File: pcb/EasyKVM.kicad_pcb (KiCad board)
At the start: 4 copper layers, 75 x 75 mm, 58 parts, among them J1 USB_A, J4 USB_B_Micro, J5 USB_B_Micro, J6 HDMI_A, J7 USB_B_Micro, J8 HDMI_A, J9 USB_A, Q1 MMBT3904, Q2 MMBT3904, Q3 BSS138, Q4 BSS138, Q5 BSS138, SW1 RESET, U1 SP0503BAHT, U2 LM3525M-H, U3 SP0503BAHT, U4 MAX4999ETJ+, U5 CP2102N-Axx-xQFN24, U6 ESP32-S3-WROOM-1, U7 SP0503BAHT, U9 AP7361C-33E

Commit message: routing start
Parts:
- added R2: 100K, Resistor_SMD:R_0603_1608Metric, F.Cu at (111.0, 104.5)
- added R3: 100K, Resistor_SMD:R_0603_1608Metric, F.Cu at (111.0, 106.6)
- added R5: 1K, Resistor_SMD:R_0603_1608Metric, F.Cu at (114.2, 108.2)
- moved D4 21.5 mm to (100.5, 138.0), turned to 90 degrees
- moved Q3 20.8 mm to (116.8, 126.1)
- moved R8 13.0 mm to (145.3, 106.5)
- moved R28 8.12 mm to (112.0, 148.4)
- moved C21 8.12 mm to (119.4, 154.9)
- moved Q1 6.51 mm to (141.4, 124.8)
- moved Q4 6.06 mm to (116.8, 130.6)
- moved C27 5.57 mm to (149.1, 123.9), turned to 90 degrees
- moved R31 5.23 mm to (145.6, 123.9), turned to -90 degrees
- moved Q2 5.22 mm to (141.4, 110.3), turned to 180 degrees
- moved R23 4.74 mm to (145.3, 110.4), turned to -90 degrees
- moved R1 2.62 mm to (114.2, 105.0), turned to 0 degrees
- moved D5 2.20 mm to (161.7, 103.9), turned to 0 degrees
- moved C2 2.05 mm to (150.9, 156.9)
- moved C30 2.03 mm to (152.3, 159.4), turned to 180 degrees
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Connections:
- D5 pad 1: ESD_PC1_USB_N -> ESD_PC1_USB_P
- D5 pad 2: ESD_PC1_USB_P -> ESD_PC1_USB_N
- D6 pad 1: ESD_PC2_USB_N -> ESD_PC2_USB_P
- D6 pad 2: ESD_PC2_USB_P -> ESD_PC2_USB_N
- U2 pad 1: KVM_ENABLE -> USB_ENABLE
- U2 pad 2: unconnected-(U2-Pad2) -> OVER_CURRENT
- U3 pad 3: HUB_USB_N -> HUB_USB_P
- U3 pad 4: HUB_USB_P -> HUB_USB_N
- U6 pad 4: unconnected-(U6-Pad4) -> OVER_CURRENT
- U6 pad 7: unconnected-(U6-Pad7) -> Net-(R5-Pad2)
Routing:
- net CHIP_PU: track 0.00 -> 88.3 mm, vias 0 -> 4
- net ESD_DDC_SDA: track 0.00 -> 57.7 mm, vias 0 -> 2
- net ESD_DDC_SCL: track 0.00 -> 56.1 mm, vias 0 -> 2
- net ESD_PC2_USB_N: track 0.00 -> 49.4 mm
- net ESD_PC2_USB_P: track 0.00 -> 49.3 mm
- net KBD_USB_N: track 0.00 -> 48.9 mm, vias 0 -> 2
- net KBD_USB_P: track 0.00 -> 48.7 mm, vias 0 -> 2
- net HDMI_5V: track 0.00 -> 45.2 mm
- net ESD_PC1_USB_N: track 0.00 -> 43.5 mm
- net ESD_PC1_USB_P: track 0.00 -> 43.4 mm
- net DDC_SCL: track 0.00 -> 42.5 mm, vias 0 -> 2
- net Net-(J6-Pad19): track 0.00 -> 40.3 mm
- net HDMI_CLK_P: track 0.00 -> 39.8 mm, vias 0 -> 2
- net DDC_SDA: track 0.00 -> 39.4 mm, vias 0 -> 2
- net ESD_USB_N: track 0.00 -> 39.2 mm, vias 0 -> 2
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
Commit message: pcb wip
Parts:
- moved R32 33.9 mm to (132.5, 122.4)
- moved R34 11.3 mm to (155.5, 120.7), turned to 0 degrees
- moved C17 11.1 mm to (155.5, 123.7), turned to 180 degrees
- moved C21 8.25 mm to (126.5, 150.7)
- moved C20 7.04 mm to (165.7, 119.5)
- moved C30 6.20 mm to (158.2, 161.5), turned to 90 degrees
- moved R36 6.17 mm to (161.1, 165.9), turned to 0 degrees
- moved R35 4.92 mm to (163.8, 160.6), turned to 180 degrees
- moved R3 3.82 mm to (108.6, 109.5)
- moved R2 3.45 mm to (108.6, 106.9)
- moved C28 2.46 mm to (113.8, 102.6), turned to 180 degrees
- moved Q5 2.37 mm to (161.1, 162.9)
- moved D1 2.33 mm to (165.7, 121.6)
- moved R22 2.26 mm to (165.7, 123.8)
- moved C11 1.99 mm to (154.3, 101.3)
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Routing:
- net GND: track 0.00 -> 168.0 mm, vias 0 -> 52
- net VBUS: track 14.8 -> 133.6 mm
- net Net-(Q5-Pad2): track 0.00 -> 63.7 mm, vias 0 -> 2
- net KVM_SELECT: track 0.00 -> 60.7 mm, vias 0 -> 2
- net OVER_CURRENT: track 0.00 -> 57.6 mm, vias 0 -> 2
- net KVM_ENABLE: track 0.00 -> 55.5 mm, vias 0 -> 2
- net USB_ENABLE: track 0.00 -> 54.7 mm, vias 0 -> 2
- net 3.3V: track 0.00 -> 35.5 mm, vias 0 -> 15
- net Net-(R34-Pad2): track 0.00 -> 23.6 mm, vias 0 -> 2
- net Net-(D3-Pad2): track 0.00 -> 20.5 mm
- net ESD_DDC_SDA: track 57.7 -> 49.6 mm
- net DDC_SCL: track 42.5 -> 48.5 mm
- net HUB_VBUS: track 21.2 -> 25.5 mm
- net DDC_SDA: track 39.4 -> 43.6 mm
- net RGB: track 0.00 -> 4.12 mm
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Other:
- board text added: "Easy KVM R1.0"

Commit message: R1
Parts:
- moved C2 0.30 mm to (150.6, 157.0)
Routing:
- net HDMI_D2_P: track 32.0 -> 38.6 mm
- net HDMI_D2_N: track 32.3 -> 38.6 mm
- net HDMI_D1_N: track 34.7 -> 38.7 mm
- net HDMI_D1_P: track 34.8 -> 38.7 mm
- net HDMI_D0_P: track 36.8 -> 38.5 mm
- net HDMI_D0_N: track 37.2 -> 38.6 mm
- net GND: track 168.0 -> 167.4 mm
- net KBD_USB_N: track 48.9 -> 49.5 mm

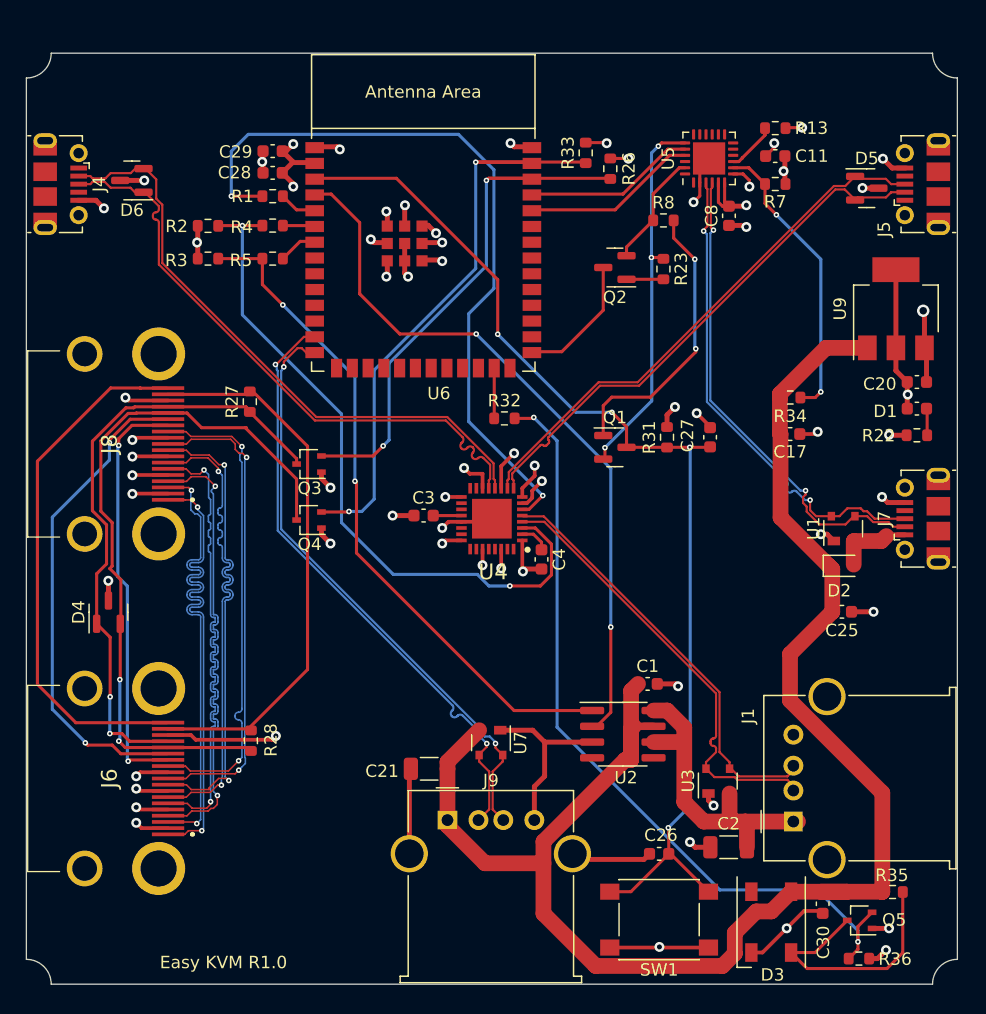
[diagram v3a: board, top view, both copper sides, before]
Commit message: design bugs case update software bugs
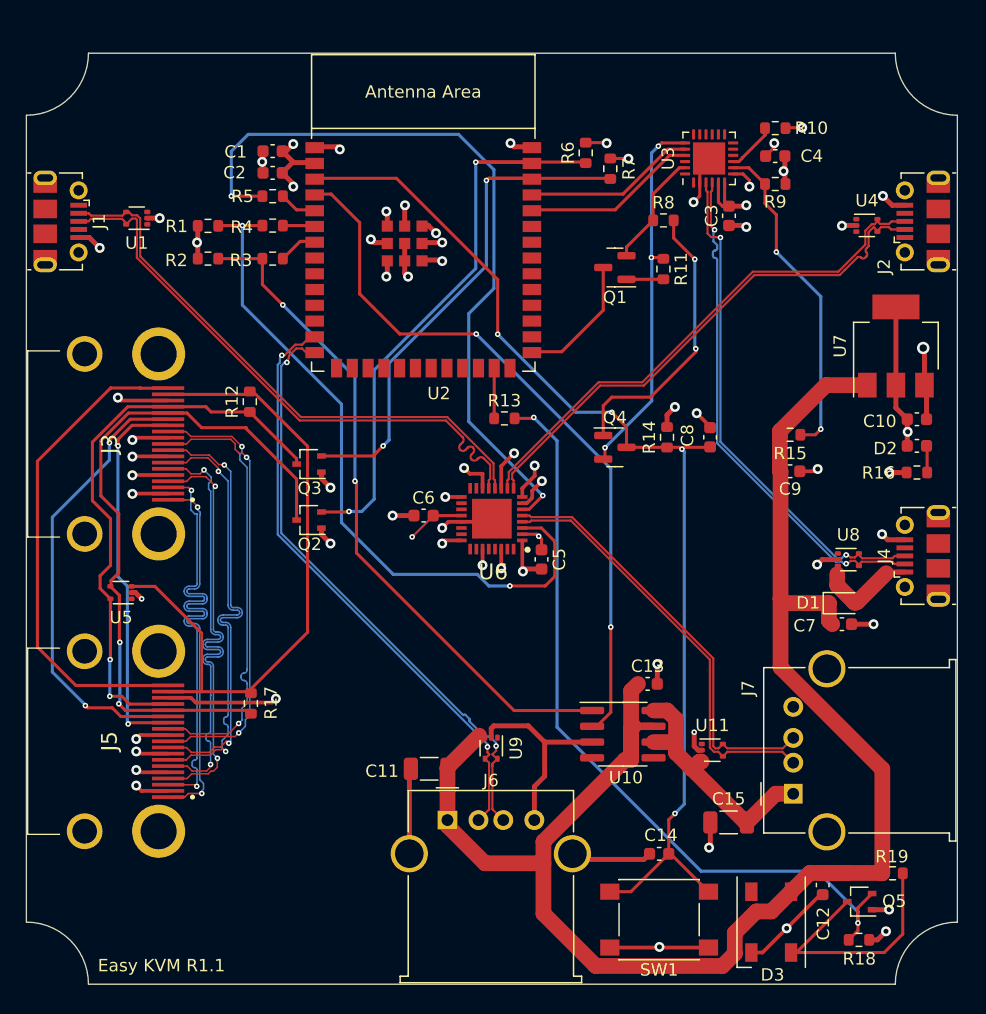
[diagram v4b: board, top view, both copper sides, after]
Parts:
- removed D4, D5, D6: SP0502BAHT, Package_TO_SOT_SMD:SOT-23
- removed the U3 at (149.7, 151.6)
- removed the U7 at (131.4, 148.5)
- added U11: SP3003-02XTG, Package_TO_SOT_SMD:Diodes_SOT-553, F.Cu at (149.3, 149.2)
- added U4: SP3003-02XTG, Package_TO_SOT_SMD:Diodes_SOT-553, F.Cu at (161.7, 106.9)
- added U5: SP3003-02XTG, Package_TO_SOT_SMD:Diodes_SOT-553, F.Cu at (101.6, 136.5)
- added U8: SP3003-02XTG, Package_TO_SOT_SMD:Diodes_SOT-553, F.Cu at (160.2, 133.8)
- added U9: SP3003-02XTG, Package_TO_SOT_SMD:Diodes_SOT-553, F.Cu at (131.4, 149.0)
- U1: value SP0503BAHT -> SP3003-02XTG; footprint Package_TO_SOT_SMD:SOT-143 -> Package_TO_SOT_SMD:Diodes_SOT-553
- moved U1 62.2 mm to (102.9, 106.3), turned to 180 degrees
- moved C10 3.00 mm to (165.7, 122.5)
- moved C9 3.00 mm to (155.5, 126.7)
- moved D1 3.00 mm to (159.7, 137.3)
- moved D2 3.00 mm to (165.7, 124.6)
- moved J1 3.00 mm to (96.8, 106.5)
- moved J2 3.00 mm to (166.2, 106.5)
- moved J4 3.00 mm to (166.2, 133.5)
- moved J5 3.00 mm to (100.2, 148.4)
- moved R15 3.00 mm to (155.5, 123.7)
- moved R16 3.00 mm to (165.7, 126.8)
- moved R17 3.00 mm to (112.1, 145.4)
- moved U7 3.00 mm to (164.1, 116.6)
- moved J7 2.24 mm to (155.8, 152.7)
- moved C15 2.00 mm to (150.6, 155.0)
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- renumbered C29 to C1, C20 to C10, C21 to C11, C30 to C12, C1 to C13, C26 to C14, C2 to C15, C28 to C2, C8 to C3, C11 to C4, C4 to C5, C3 to C6, C25 to C7, C27 to C8, C17 to C9, D2 to D1, D1 to D2, J4 to J1, J5 to J2, J8 to J3, J7 to J4, J6 to J5, J9 to J6, J1 to J7, Q2 to Q1, Q4 to Q2, Q1 to Q4, R2 to R1, R13 to R10, R23 to R11, R27 to R12, R32 to R13, R31 to R14, R34 to R15, R22 to R16, R28 to R17, R36 to R18, R35 to R19, R3 to R2, R5 to R3, R1 to R5, R33 to R6, R26 to R7, R7 to R9, U2 to U10, U6 to U2, U5 to U3, U4 to U6, U9 to U7
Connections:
- C5 pad 1: Net-(C4-Pad1) -> 3.3V
- C6 pad 2: Net-(C3-Pad2) -> 3.3V
- J7 pad 5: unconnected-(J1-Pad5) -> GND
- U1 pad 1: GND -> unconnected-(U7-Pad1)
- U1 pad 2: ESD_VBUS -> GND
- U1 pad 3: ESD_USB_N -> unconnected-(U7-Pad3)
- U1 pad 4: ESD_USB_P -> ESD_PC2_USB_N
- U6 pad 2: Net-(C4-Pad1) -> 3.3V
- U6 pad 20: Net-(C3-Pad2) -> 3.3V
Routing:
- net HDMI_5V: track 44.0 -> 52.9 mm
- net 3.3V: track 35.5 -> 42.7 mm, vias 15 -> 17
- net HUB_VBUS: track 25.5 -> 20.4 mm
- net ESD_PC2_USB_N: track 49.5 -> 45.9 mm
- net ESD_DDC_SDA: track 49.6 -> 46.5 mm
- net Net-(R34-Pad2): track 23.6 -> 26.6 mm
- net Net-(J6-Pad14): track 39.7 -> 36.7 mm
- net Net-(J6-Pad13): track 34.0 -> 31.0 mm
- net Net-(J6-Pad19): track 42.6 -> 39.6 mm
- net HDMI_CLK_P: track 39.0 -> 36.2 mm
- net HDMI_CLK_N: track 39.0 -> 36.2 mm
- net HDMI_D1_P: track 38.7 -> 36.0 mm
- net ESD_DDC_SCL: track 57.9 -> 55.2 mm
- net HDMI_D2_P: track 38.6 -> 36.1 mm
- net HDMI_D0_N: track 38.6 -> 36.1 mm
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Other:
- outline, holes or cut-outs redrawn
- board text added: "Easy KVM R1.1"
- board text removed: "Easy KVM R1.0"

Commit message: Fix cornerns Add hub diode R3
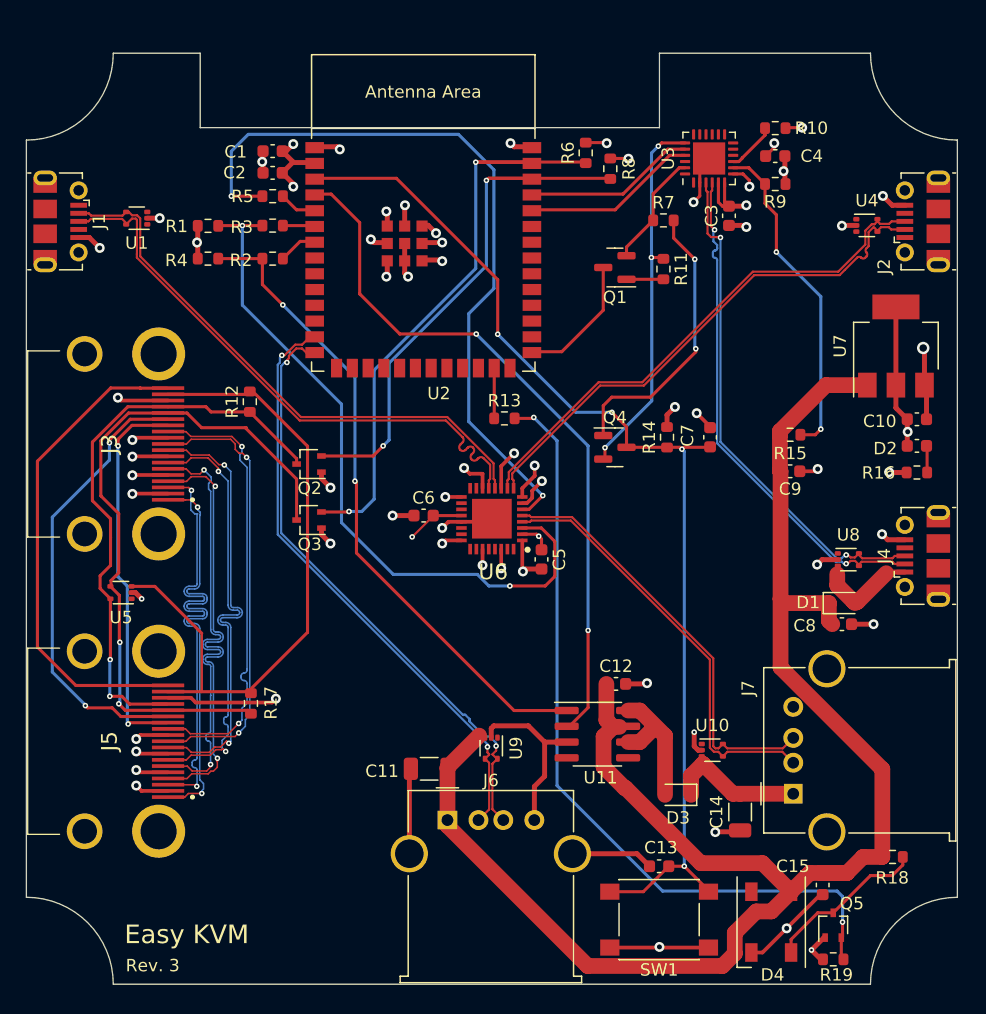
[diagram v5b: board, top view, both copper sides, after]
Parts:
- added D3: 1N5819, Diode_SMD:D_SOD-323, F.Cu at (146.5, 152.8)
- moved Q5 2.85 mm to (159.0, 163.2), turned to 90 degrees
- moved R19 2.60 mm to (159.0, 166.0), turned to 180 degrees
- moved C12 2.55 mm to (141.5, 143.8)
- moved U11 2.05 mm to (140.0, 147.9)
- moved R18 1.31 mm to (163.8, 157.8)
- moved C14 1.25 mm to (151.5, 154.1), turned to 90 degrees
- moved C13 1.00 mm to (145.0, 158.5)
- renumbered C13 to C12, C14 to C13, C15 to C14, C12 to C15, C8 to C7, C7 to C8, D3 to D4, Q3 to Q2, Q2 to Q3, R19 to R18, R18 to R19, R3 to R2, R4 to R3, R2 to R4, R8 to R7, R7 to R8, U11 to U10, U10 to U11
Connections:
- U11 pad 6: HUB_VBUS -> Net-(U10-Pad6)
- U11 pad 8: HUB_VBUS -> Net-(U10-Pad6)
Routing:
- net Net-(U10-Pad6): track 0.00 -> 11.0 mm
- net HUB_VBUS: track 20.4 -> 11.2 mm
- net Net-(D3-Pad2): track 20.7 -> 13.2 mm
- net USB_ENABLE: track 54.7 -> 52.6 mm
- net GND: track 169.7 -> 167.9 mm
- net VBUS: track 132.4 -> 133.9 mm
- net Net-(Q5-Pad2): track 63.1 -> 63.9 mm
- net 3.3V: track 42.7 -> 42.4 mm, vias 17 -> 16
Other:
- outline, holes or cut-outs redrawn
- board text added: "Easy KVM"
- board text added: "Rev. 3"
- board text removed: "Easy KVM R1.1"
